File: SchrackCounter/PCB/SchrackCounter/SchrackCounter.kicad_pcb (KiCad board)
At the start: 4 copper layers, 98 x 88 mm, 61 parts, among them J1 Conn_01x02_Pin, J2 TYPE-C-31-M-12 (USB C CONN), J3 MEM2067-02-180-00-A_REVB, SW1 SW_Push, SW2 SW_Push, SW3 SW_Push, SW4 SW_Push, SW5 SW_Push, U1 LM1084-3.3, U2 LDD080BUE-101A, U3 LTD080BUE-103A, U4 LDD080BUE-101A, U5 MAX7219, U6 ESP32-S3-WROOM-2, U7 USBLC6-2SC6

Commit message: Schrack pcb updates
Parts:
- U5: footprint Package_SO:SOIC-24W_7.5x15.4mm_P1.27mm -> Package_DIP:DIP-24_W10.16mm; moved to F.Cu
- moved U5 225.1 mm to (1.07, 1.57), turned to 0 degrees

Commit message: bom final, schematic updates
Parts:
- moved TP2 69.1 mm to (361.8, 80.7)
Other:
- board text added: "Switches used in SchrackCounter PCB: - MAIN POWER SWITCH (Rotary switch used for power supp) - MODE: Optional switch for other software purpose (modes, time, etc) - RESET: Score/Time reset - Time is set using a webserver"
- board text removed: "Who and how will make holes for the Schrack buttons, Dimensions needed: - Schrack tactile switches - Schrack light switch (the main premise)"
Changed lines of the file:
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@@
 	(footprint "sumec_graphic:SCHRACK_LOGO_IMG"
 		(layer "F.Cu")
-		(at 304.5 42)
+		(at 361.764 80.684)
 		(property "Reference" "TP2"
 			(at 0 0 0)
@@
 		(layer "Edge.Cuts")
 	)
-	(gr_text "Who and how will make holes for the Schrack buttons,\nDimensions needed: \n- Schrack tactile switches\n- Schrack light switch (the main premise)"
-		(at 73.75 256.25 0)
+	(gr_text "Switches used in SchrackCounter PCB:\n- MAIN POWER SWITCH (Rotary switch used for power supp)\n- MODE: Optional switch for other software purpose (modes, time, etc)\n- RESET: Score/Time reset\n- Time is set using a webserver"
+		(at 149.166 237.656 0)
 		(layer "Cmts.User")
 		(effects
@@
 	)
 	(gr_text "POWER"
-		(at 194.25 188 0)
+		(at 196.156 187.11 0)
 		(layer "Cmts.User")
 		(effects
@@
 	)
 	(gr_text "MODE"
-		(at 148.75 176.5 0)
+		(at 152.722 176.188 0)
 		(layer "Cmts.User")
 		(effects
@@
 	)
 	(gr_text "RESET"
-		(at 240.75 176.25 0)
+		(at 241.622 175.172 0)
 		(layer "Cmts.User")
 		(effects

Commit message: PCB update, minor schematic update
PCB routing update, 7segment routing, and minor changes to the 7segments in schematic
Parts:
- moved U5 257.7 mm to (241.8, 93.3), turned to 180 degrees
- moved TP1 64.5 mm to (353.5, 47.6)
- moved C5 53.8 mm to (235.8, 82.2)
- moved R1 52.2 mm to (233.8, 77.9)
- moved C6 50.7 mm to (233.8, 81.6)
- moved BZ1 35.2 mm to (217.8, 100.3)
- moved R5 33.9 mm to (217.8, 110.1), turned to 180 degrees
- moved D3 18.7 mm to (215.2, 119.3), turned to -90 degrees
- moved D2 18.4 mm to (220.2, 119.3), turned to -90 degrees
- moved R8 17.8 mm to (217.8, 119.3), turned to -90 degrees
- moved C9 13.3 mm to (235.1, 99.9)
- moved D1 13.3 mm to (234.5, 102.1)
- moved J2 13.3 mm to (243.2, 103.6)
- moved R6 13.3 mm to (235.1, 104.3)
- moved R7 13.3 mm to (235.1, 106.3)
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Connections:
- U2 pad 4: DP1 -> DP0
- U2 pad 9: DP2 -> DP1
- U3 pad 6: DPX -> DP4-6
- U4 pad 4: DP3 -> DP2
- U4 pad 9: DP4 -> DP3
- U5 pad 10: DP5 -> unconnected-(U5-DIG_5-Pad10)
- U5 pad 11: DP1 -> unconnected-(U5-DIG_1-Pad11)
- U5 pad 2: DP0 -> DP4-6
- U5 pad 3: DP4 -> DP0
- U5 pad 5: DP6 -> DP1
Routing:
- net SEG_G: track 0.00 -> 131.3 mm, vias 0 -> 5
- net SEG_A: track 0.00 -> 125.3 mm, vias 0 -> 5
- net SEG_B: track 0.00 -> 121.9 mm, vias 0 -> 5
- net +3V3: track 0.00 -> 121.0 mm, vias 0 -> 1
- net SEG_F: track 0.00 -> 119.4 mm, vias 0 -> 5
- net SEG_E: track 0.00 -> 110.5 mm, vias 0 -> 5
- net SEG_C: track 0.00 -> 107.9 mm, vias 0 -> 4
- net SEG_D: track 0.00 -> 92.5 mm, vias 0 -> 4
- net DP0: track 0.00 -> 79.4 mm
- net DP1: track 0.00 -> 70.4 mm
- net DP4-6: track 0.00 -> 63.9 mm
- net DP2: track 0.00 -> 47.8 mm
- net DP3: track 0.00 -> 36.3 mm
- net +5V: track 0.00 -> 23.4 mm
- net VBATT: track 0.00 -> 11.3 mm
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
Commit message: pcb routing update
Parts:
- moved R12 13.0 mm to (240.2, 122.3)
- moved C13 0.95 mm to (236.8, 133.8)
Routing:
- net +3V3: track 121.0 -> 75.0 mm
- net BZ1_PWM: track 0.00 -> 11.6 mm
- net D+: track 0.00 -> 9.21 mm, vias 0 -> 1
- net D-: track 0.00 -> 6.81 mm, vias 0 -> 1
- net VBUS 5V: track 0.00 -> 6.41 mm, vias 0 -> 1
- net BOOT: track 0.00 -> 6.00 mm, vias 0 -> 1
- net Net-(BZ1-+): track 0.00 -> 2.66 mm
- net Net-(R7-Pad2): track 0.00 -> 0.82 mm, vias 0 -> 1
- net Net-(R6-Pad2): track 0.00 -> 0.82 mm, vias 0 -> 1
- net EN: track 0.00 -> 0.80 mm, vias 0 -> 1
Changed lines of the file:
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@@
 		(tags "THT DIP DIL PDIP 2.54mm 10.16mm 400mil")
 		(property "Reference" "U5"
-			(at 5.08 -2.33 360)
+			(at 5.08 -2.33 0)
 			(layer "F.SilkS")
 			(effects
@@
 		)
 		(property "Value" "MAX7219"
-			(at 5.08 30.27 360)
+			(at 5.08 30.27 0)
 			(layer "F.Fab")
 			(effects
@@
 		)
 		(fp_text user "${REFERENCE}"
-			(at 5.08 13.97 360)
+			(at 5.08 13.97 0)
 			(layer "F.Fab")
 			(effects
@@
 		(tags "resistor handsolder")
 		(property "Reference" "R5"
-			(at 0 -1.65 360)
+			(at 0 -1.65 0)
 			(layer "F.SilkS")
 			(effects
@@
 		)
 		(property "Value" "0R"
-			(at 0 1.65 360)
+			(at 0 1.65 0)
 			(layer "F.Fab")
 			(effects
@@
 		)
 		(fp_text user "${REFERENCE}"
-			(at 0 0 360)
+			(at 0 0 0)
 			(layer "F.Fab")
 			(effects
@@
 		(at 212.65 130.03)
 		(property "Reference" "J3"
-			(at -2.02289 -8.47815 360)
+			(at -2.02289 -8.47815 0)
 			(layer "F.SilkS")
 			(effects
@@
 		)
 		(property "Value" "MEM2067-02-180-00-A_REVB"
-			(at 21.47881 8.54627 360)
+			(at 21.47881 8.54627 0)
 			(layer "F.Fab")
 			(effects
@@
 		)
 		(property "Footprint" "Schrack_brd:MICRO_SD_CARD"
-			(at 0 0 360)
+			(at 0 0 0)
 			(layer "F.Fab")
 			(hide yes)
@@
 		)
 		(property "Datasheet" ""
-			(at 0 0 360)
+			(at 0 0 0)
 			(layer "F.Fab")
 			(hide yes)
@@
 		)
 		(property "Description" ""
-			(at 0 0 360)
+			(at 0 0 0)
 			(layer "F.Fab")
 			(hide yes)
@@
 	(footprint "Resistor_SMD:R_0805_2012Metric_Pad1.20x1.40mm_HandSolder"
 		(layer "B.Cu")
-		(at 236.8 134.88 180)
+		(at 240.15 122.33 180)
 		(descr "Resistor SMD 0805 (2012 Metric), square (rectangular) end terminal, IPC_7351 nominal with elongated pad for handsoldering. (Body size source: IPC-SM-782 page 72, https://www.pcb-3d.com/wordpress/wp-content/uploads/ipc-sm-782a_amendment_1_and_2.pdf), generated with kicad-footprint-generator")
 		(tags "resistor handsolder")
@@
 	(footprint "Capacitor_SMD:C_0805_2012Metric_Pad1.18x1.45mm_HandSolder"
 		(layer "B.Cu")
-		(at 236.8 132.88 180)
+		(at 236.75 133.83 180)
 		(descr "Capacitor SMD 0805 (2012 Metric), square (rectangular) end terminal, IPC_7351 nominal with elongated pad for handsoldering. (Body size source: IPC-SM-782 page 76, https://www.pcb-3d.com/wordpress/wp-content/uploads/ipc-sm-782a_amendment_1_and_2.pdf, https://docs.google.com/spreadsheets/d/1BsfQQcO9C6DZCsRaXUlFlo91Tg2WpOkGARC1WS5S8t0/edit?usp=sharing), generated with kicad-footprint-generator")
 		(tags "capacitor handsolder")
@@
 	)
 	(segment
-		(start 233.8038 134.88)
-		(end 235.8 134.88)
-		(width 0.25)
-		(layer "B.Cu")
-		(net 4)
-	)
-	(segment
-		(start 227.7538 128.83)
-		(end 233.8038 134.88)
-		(width 0.25)
-		(layer "B.Cu")
-		(net 4)
-	)
-	(segment
 		(start 199.125 130.375)
 		(end 200.25 129.25)
@@
 	)
 	(segment
-		(start 215 128.83)
-		(end 227.7538 128.83)
-		(width 0.25)
-		(layer "B.Cu")
-		(net 4)
-	)
-	(segment
 		(start 170.13 100.8725)
 		(end 174.0375 104.78)
@@
 	)
 	(segment
-		(start 241.7675 114.8163)
-		(end 227.7538 128.83)
-		(width 0.25)
-		(layer "B.Cu")
-		(net 4)
-	)
-	(segment
 		(start 170.13 92.58)
 		(end 170.13 100.8725)
@@
 	)
 	(segment
-		(start 241.7675 111.94)
-		(end 241.7675 114.8163)
-		(width 0.25)
-		(layer "B.Cu")
-		(net 4)
-	)
-	(segment
 		(start 212.6 131.2675)
 		(end 212.6 133.38)
@@
 	)
 	(segment
+		(start 231.75 103.355)
+		(end 231.75 105.33)
+		(width 0.5)
+		(layer "F.Cu")
+		(net 5)
+	)
+	(segment
+		(start 233.025 102.08)
+		(end 231.75 103.355)
+		(width 0.5)
+		(layer "F.Cu")
+		(net 5)
+	)
+	(segment
+		(start 234.075 101.03)
+		(end 233.025 102.08)
+		(width 0.5)
+		(layer "F.Cu")
+		(net 5)
+	)
+	(segment
+		(start 234.075 99.88)
+		(end 234.075 101.03)
+		(width 0.5)
+		(layer "F.Cu")
+		(net 5)
+	)
+	(via
+		(at 231.75 105.33)
+		(size 0.7)
+		(drill 0.3)
+		(layers "F.Cu" "B.Cu")
+		(net 5)
+	)
+	(segment
+		(start 238.65 133.83)
+		(end 239.45 133.83)
+		(width 0.25)
+		(layer "F.Cu")
+		(net 6)
+	)
+	(via
+		(at 238.65 133.83)
+		(size 0.7)
+		(drill 0.3)
+		(layers "F.Cu" "B.Cu")
+		(net 6)
+	)
+	(segment
+		(start 226.59 133.24)
+		(end 226.59 129.19)
+		(width 0.25)
+		(layer "F.Cu")
+		(net 7)
+	)
+	(segment
+		(start 224.8875 133.83)
+		(end 226 133.83)
+		(width 0.25)
+		(layer "F.Cu")
+		(net 7)
+	)
+	(segment
+		(start 226 133.83)
+		(end 226.59 133.24)
+		(width 0.25)
+		(layer "F.Cu")
+		(net 7)
+	)
+	(via
+		(at 226 133.83)
+		(size 0.7)
+		(drill 0.3)
+		(layers "F.Cu" "B.Cu")
+		(net 7)
+	)
+	(segment
 		(start 236.9 101.18)
 		(end 238.4125 101.18)
@@
 		(net 25)
 	)
+	(via
+		(at 226.6 110.98)
+		(size 0.6)
+		(drill 0.25)
+		(layers "F.Cu" "B.Cu")
+		(net 29)
+	)
+	(segment
+		(start 230.9525 104.38)
+		(end 229.575 104.38)
+		(width 0.25)
+		(layer "B.Cu")
+		(net 29)
+	)
+	(segment
+		(start 229.575 104.38)
+		(end 226.6 107.355)
+		(width 0.25)
+		(layer "B.Cu")
+		(net 29)
+	)
+	(segment
+		(start 226.6 107.355)
+		(end 226.6 110.98)
+		(width 0.25)
+		(layer "B.Cu")
+		(net 29)
+	)
+	(via
+		(at 227.85 110.98)
+		(size 0.6)
+		(drill 0.25)
+		(layers "F.Cu" "B.Cu")
+		(net 30)
+	)
+	(segment
+		(start 230.9525 106.28)
+		(end 229.55 106.28)
+		(width 0.25)
+		(layer "B.Cu")
+		(net 30)
+	)
+	(segment
+		(start 227.85 107.98)
+		(end 227.85 110.98)
+		(width 0.25)
+		(layer "B.Cu")
+		(net 30)
+	)
+	(segment
+		(start 229.55 106.28)
+		(end 227.85 107.98)
+		(width 0.25)
+		(layer "B.Cu")
+		(net 30)
+	)
 	(segment
 		(start 191 131.25)
@@
 	)
 	(segment
+		(start 229.13 111.69)
+		(end 229.13 110.69)
+		(width 0.25)
+		(layer "F.Cu")
+		(net 37)
+	)
+	(segment
+		(start 228.52 110.08)
+		(end 218.75 110.08)
+		(width 0.25)
+		(layer "F.Cu")
+		(net 37)
+	)
+	(segment
+		(start 229.13 110.69)
+		(end 228.52 110.08)
+		(width 0.25)
+		(layer "F.Cu")
+		(net 37)
+	)
+	(segment
 		(start 238.75 92.83)
 		(end 234.75 96.83)
@@
 	)
 	(segment
+		(start 216.75 110.08)
+		(end 216.75 108.83)
+		(width 0.25)
+		(layer "F.Cu")
+		(net 62)
+	)
+	(segment
+		(start 216.75 108.83)
+		(end 217.75 107.83)
+		(width 0.25)
+		(layer "F.Cu")
+		(net 62)
+	)
+	(segment
 		(start 182.75 126.83)
 		(end 182.75 124.555)
@@
 		(net 65)
 	)
+	(via
+		(at 233.55 104.38)
+		(size 0.6)
+		(drill 0.25)
+		(layers "F.Cu" "B.Cu")
+		(net 71)
+	)
+	(segment
+		(start 234.3725 104.38)
+		(end 233.55 104.38)
+		(width 0.25)
+		(layer "B.Cu")
+		(net 71)
+	)
+	(via
+		(at 233.55 106.28)
+		(size 0.6)
+		(drill 0.25)
+		(layers "F.Cu" "B.Cu")
+		(net 72)
+	)
+	(segment
+		(start 234.3725 106.28)
+		(end 233.55 106.28)
+		(width 0.25)
+		(layer "B.Cu")
+		(net 72)
+	)
 )

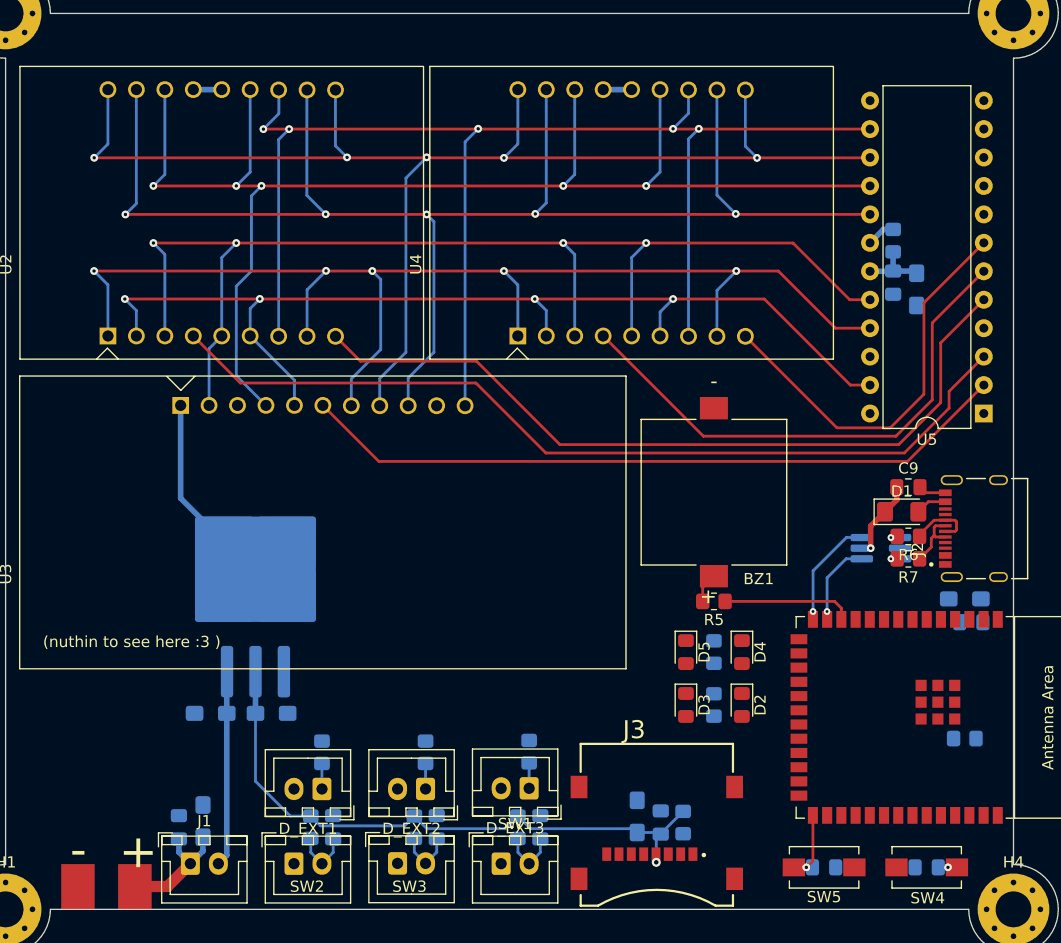
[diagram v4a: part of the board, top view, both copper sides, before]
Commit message: minor routing update
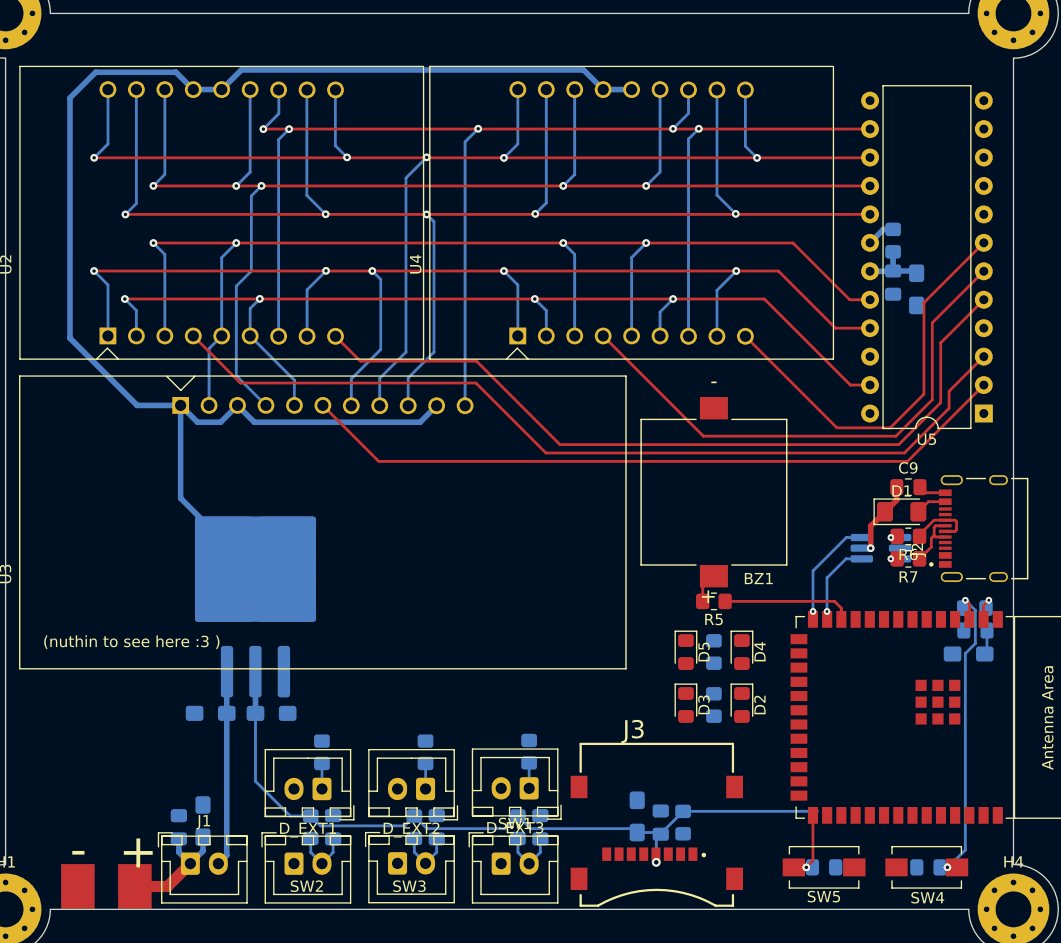
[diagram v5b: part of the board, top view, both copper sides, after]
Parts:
- moved R12 11.7 mm to (241.1, 110.7), turned to 0 degrees
- moved C7 4.93 mm to (240.5, 114.8)
- moved C8 0.83 mm to (241.1, 112.7)
- moved C13 0.15 mm to (236.9, 133.8)
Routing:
- net +3V3: track 75.0 -> 201.3 mm, vias 1 -> 2
- net EN: track 0.80 -> 28.7 mm, vias 1 -> 2

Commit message: SchrackCounter
PCB Finished
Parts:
- added U8: DC56-11CGKWA, Display_7Segment:DA56-11CGKWA, F.Cu at (130.2, 82.6)
- C1: renamed from C3; value 10uF.stabl -> 10uF
- C4: value 10uF.stabl -> 10uF
- C5: value 10uF.max -> 10uF
- C6: value 100nF.max -> 100nF
- C7: value 10uF.mcu -> 10uF
- C8: value 100nF.mcu -> 100nF
- moved TP1 209.6 mm to (159.5, 126.8)
- moved TP2 200.0 mm to (166.0, 121.8)
- moved U1 14.7 mm to (162.3, 111.6), turned to 180 degrees
- moved C4 11.7 mm to (173.8, 109.3), turned to 90 degrees
- moved C1 5.58 mm to (173.8, 114.6), turned to -90 degrees
- moved C15 5.28 mm to (211.8, 134.5), turned to -90 degrees
- moved C16 4.15 mm to (213.9, 133.9), turned to -90 degrees
- moved R14 4.15 mm to (215.9, 133.9), turned to -90 degrees
- moved D5 3.71 mm to (222.0, 111.3)
- moved D4 3.51 mm to (214.0, 111.3)
- moved R2 3.38 mm to (185.0, 126.1), turned to -90 degrees
- moved R3 3.38 mm to (194.2, 126.1), turned to -90 degrees
- moved R9 3.28 mm to (218.0, 111.3)
- moved D2 2.47 mm to (222.0, 117.6)
- moved D3 2.15 mm to (214.0, 117.6)
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- renumbered C11 to C10, C12 to C11, C13 to C12, C10 to C13, C1 to C2, C2 to C3, D5 to D4, D4 to D5, R11 to R10, R13 to R11, R10 to R13, SW2 to SW1, SW3 to SW2, SW1 to SW3
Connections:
- U6 pad 17: RED_FLASH -> GREEN_FLASH
- U6 pad 18: ~{CS0} -> MISO
- U6 pad 19: MOSI -> CLK
- U6 pad 20: MISO -> MOSI
- U6 pad 21: CLK -> ~{CS1}
- U6 pad 22: ~{CS1} -> RED_FLASH
- U6 pad 23: GREEN_FLASH -> LED_EXT3
- U6 pad 31: unconnected-(U6-IO38-Pad31) -> LED_EXT2
- U6 pad 32: LED_EXT3 -> LED_EXT1
- U6 pad 33: LED_EXT2 -> MODE
- U6 pad 34: LED_EXT1 -> SCHRACK_SW
- U6 pad 38: SCHRACK_SW -> unconnected-(U6-IO2-Pad38)
- U6 pad 39: MODE -> unconnected-(U6-IO1-Pad39)
- U6 pad 4: unconnected-(U6-IO4-Pad4) -> ~{CS0}
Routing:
- net +5V: track 23.4 -> 106.3 mm, vias 0 -> 5
- net CLK: track 0.00 -> 77.2 mm, vias 0 -> 2
- net MODE: track 5.29 -> 61.5 mm
- net MOSI: track 0.00 -> 52.5 mm, vias 0 -> 2
- net LED_EXT1: track 0.00 -> 51.8 mm, vias 0 -> 1
- net ~{CS0}: track 0.00 -> 49.0 mm
- net SCHRACK_SW: track 5.24 -> 53.5 mm
- net LED_EXT2: track 0.00 -> 40.8 mm, vias 0 -> 1
- net RESET: track 5.29 -> 45.5 mm
- net +3V3: track 201.3 -> 240.1 mm, vias 2 -> 4
- net LED_EXT3: track 0.00 -> 24.6 mm, vias 0 -> 1
- net MISO: track 0.00 -> 22.6 mm, vias 0 -> 2
- net ~{CS1}: track 0.00 -> 18.0 mm, vias 0 -> 2
- net RED_FLASH: track 0.00 -> 9.54 mm, vias 0 -> 1
- net GREEN_FLASH: track 0.00 -> 9.48 mm, vias 0 -> 1
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- added copper zone on B.Cu, net GND
- added copper zone on F.Cu, net GND
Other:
- board text added: "MADE BY SAVVA POPOV"

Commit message: fixes to be made
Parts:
- moved TP1 5.76 mm to (165.2, 127.1)

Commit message: PCB and Schematic updates
Fixed 7seg footprints, common cathode, fixed pinout.

PCB razed and started from scratch
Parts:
- removed U8: DC56-11CGKWA, Display_7Segment:DA56-11CGKWA
- U2, U4: value LDD080BUE-101A -> LDD080AUE-101A; footprint Schrack_brd:LDD080BUE-101A_made_by_bismarx -> Schrack_brd:WENRUN_LDD080x_7segment_2dig
- U3: value LTD080BUE-103A -> LTD080AUE-103A; footprint Schrack_brd:LTD080BUE-103A_made_by_bismarx -> Schrack_brd:WENRUN_LTD080x_7segment_3dig
- U6: moved to B.Cu
- moved TP1 77.4 mm to (241.5, 113.6), turned to 90 degrees
- moved TP2 71.8 mm to (236.2, 107.1), turned to 90 degrees
- moved R10 67.5 mm to (248.8, 121.8), turned to -90 degrees
- moved C10 63.6 mm to (246.8, 121.8), turned to 90 degrees
- moved SW1 62.1 mm to (241.5, 123.0), turned to 180 degrees
- moved U6 61.2 mm to (294.0, 104.6), turned to 0 degrees
- moved J2 54.6 mm to (199.5, 136.3), turned to 0 degrees
- moved BZ1 52.8 mm to (270.5, 100.3)
- moved R5 52.8 mm to (270.8, 110.1)
- moved SW2 52.1 mm to (241.5, 130.4), turned to 180 degrees
- moved C11 47.6 mm to (240.5, 126.9)
- moved R11 47.6 mm to (238.5, 126.9)
- moved R7 44.2 mm to (196.8, 128.3), turned to 90 degrees
- moved R6 43.5 mm to (198.8, 128.3), turned to 90 degrees
- moved C9 42.7 mm to (203.1, 128.3), turned to -90 degrees
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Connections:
- U2 pad 10: SEG_F -> SEG_B
- U2 pad 11: SEG_G -> SEG_A
- U2 pad 12: SEG_B -> SEG_F
- U2 pad 13: +3V3 -> DIG_1
- U2 pad 14: +3V3 -> DIG_0
- U2 pad 4: DP0 -> SEG_DP
- U2 pad 5: SEG_C -> SEG_E
- U2 pad 7: SEG_A -> SEG_G
- U2 pad 8: SEG_E -> SEG_C
- U2 pad 9: DP1 -> SEG_DP
- U3 pad 1: +3V3 -> DIG_4
- U3 pad 10: +3V3 -> DIG_6
- U3 pad 3: +3V3 -> DIG_5
- U3 pad 6: DP4-6 -> SEG_DP
- U4 pad 10: SEG_F -> SEG_B
- U4 pad 11: SEG_G -> SEG_A
- U4 pad 12: SEG_B -> SEG_F
- U4 pad 13: +3V3 -> DIG_3
- U4 pad 14: +3V3 -> DIG_2
- U4 pad 4: DP2 -> SEG_DP
- U4 pad 5: SEG_C -> SEG_E
- U4 pad 7: SEG_A -> SEG_G
- U4 pad 8: SEG_E -> SEG_C
- U4 pad 9: DP3 -> SEG_DP
- U5 pad 10: unconnected-(U5-DIG_5-Pad10) -> DIG_5
- U5 pad 11: unconnected-(U5-DIG_1-Pad11) -> DIG_1
- U5 pad 2: DP4-6 -> DIG_0
- U5 pad 22: unconnected-(U5-SEG_DP-Pad22) -> SEG_DP
- U5 pad 3: DP0 -> DIG_4
- U5 pad 5: DP1 -> DIG_6
- U5 pad 6: DP2 -> DIG_2
- U5 pad 7: DP3 -> DIG_3
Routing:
- net +3V3: track 240.1 -> 107.9 mm
- net DP0: track 79.3 -> 0.00 mm
- net SEG_DP: track 0.00 -> 75.6 mm
- net +5V: track 106.3 -> 31.5 mm, vias 5 -> 2
- net DP1: track 70.4 -> 0.00 mm
- net DP4-6: track 63.4 -> 0.00 mm
- net SEG_G: track 132.6 -> 71.4 mm, vias 5 -> 0
- net SEG_A: track 126.5 -> 69.5 mm, vias 5 -> 0
- net SEG_B: track 123.1 -> 71.2 mm, vias 5 -> 0
- net SEG_F: track 120.7 -> 70.2 mm, vias 5 -> 0
- net DP2: track 47.8 -> 0.00 mm
- net SEG_E: track 111.7 -> 74.2 mm, vias 5 -> 0
- net DP3: track 36.3 -> 0.00 mm
- net SEG_C: track 109.1 -> 73.0 mm, vias 4 -> 0
- net SEG_D: track 93.7 -> 70.1 mm, vias 4 -> 0
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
